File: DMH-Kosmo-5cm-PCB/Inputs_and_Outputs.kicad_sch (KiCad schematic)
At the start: 7 parts, among them J1 TS_Jack_6.35mm_Sw, J2 TS_Jack_6.35mm_Sw, J200 IDC_02x05, J3 TS_Jack_6.35mm_Sw, J4 TS_Jack_6.35mm_Sw, J50 Conn_01x06, J60 Conn_01x06

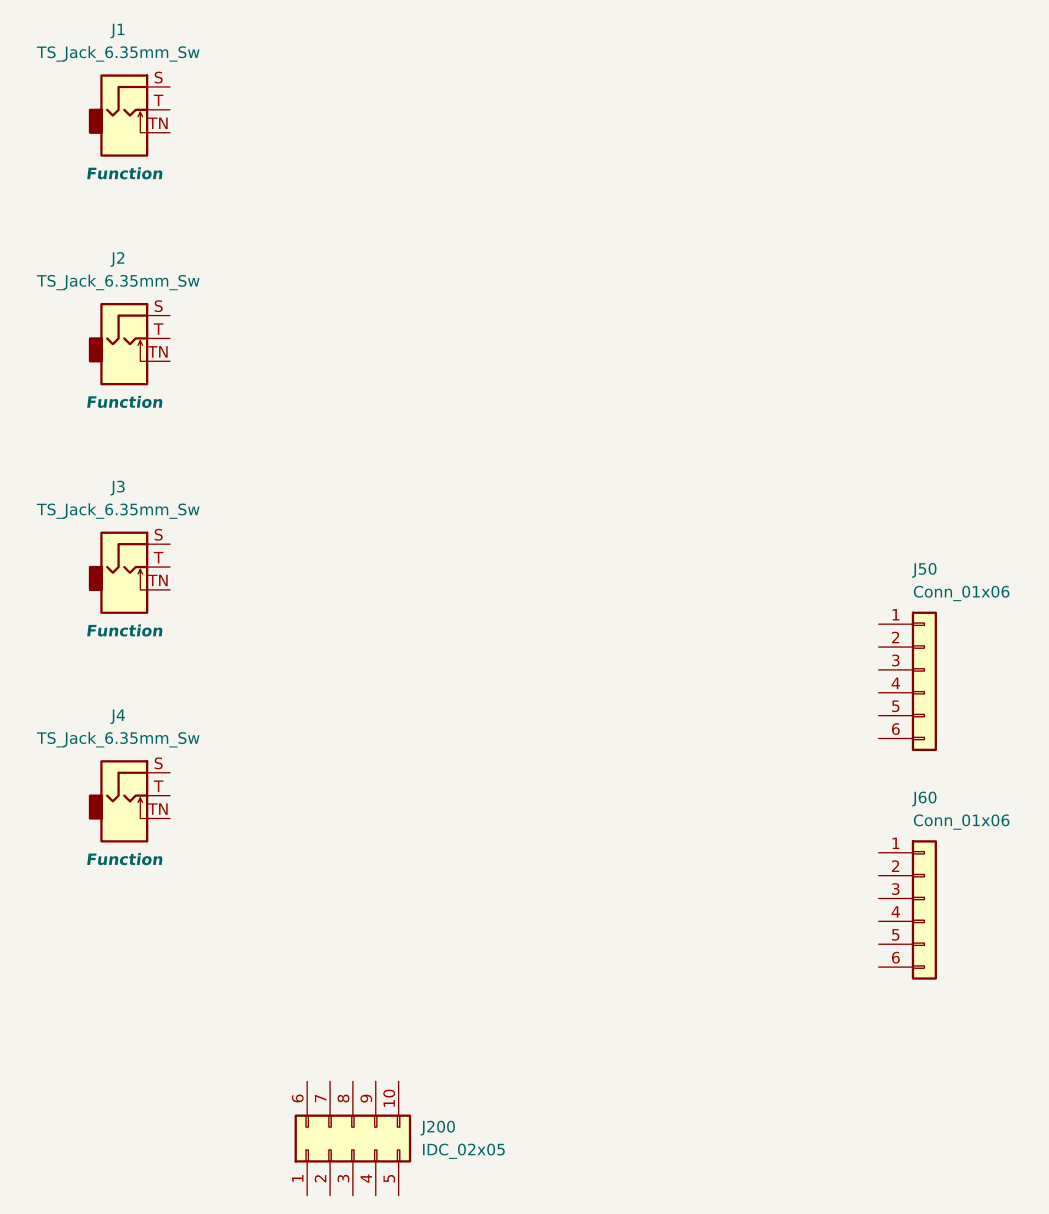
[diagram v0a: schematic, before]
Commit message: Enlarged PCB limits
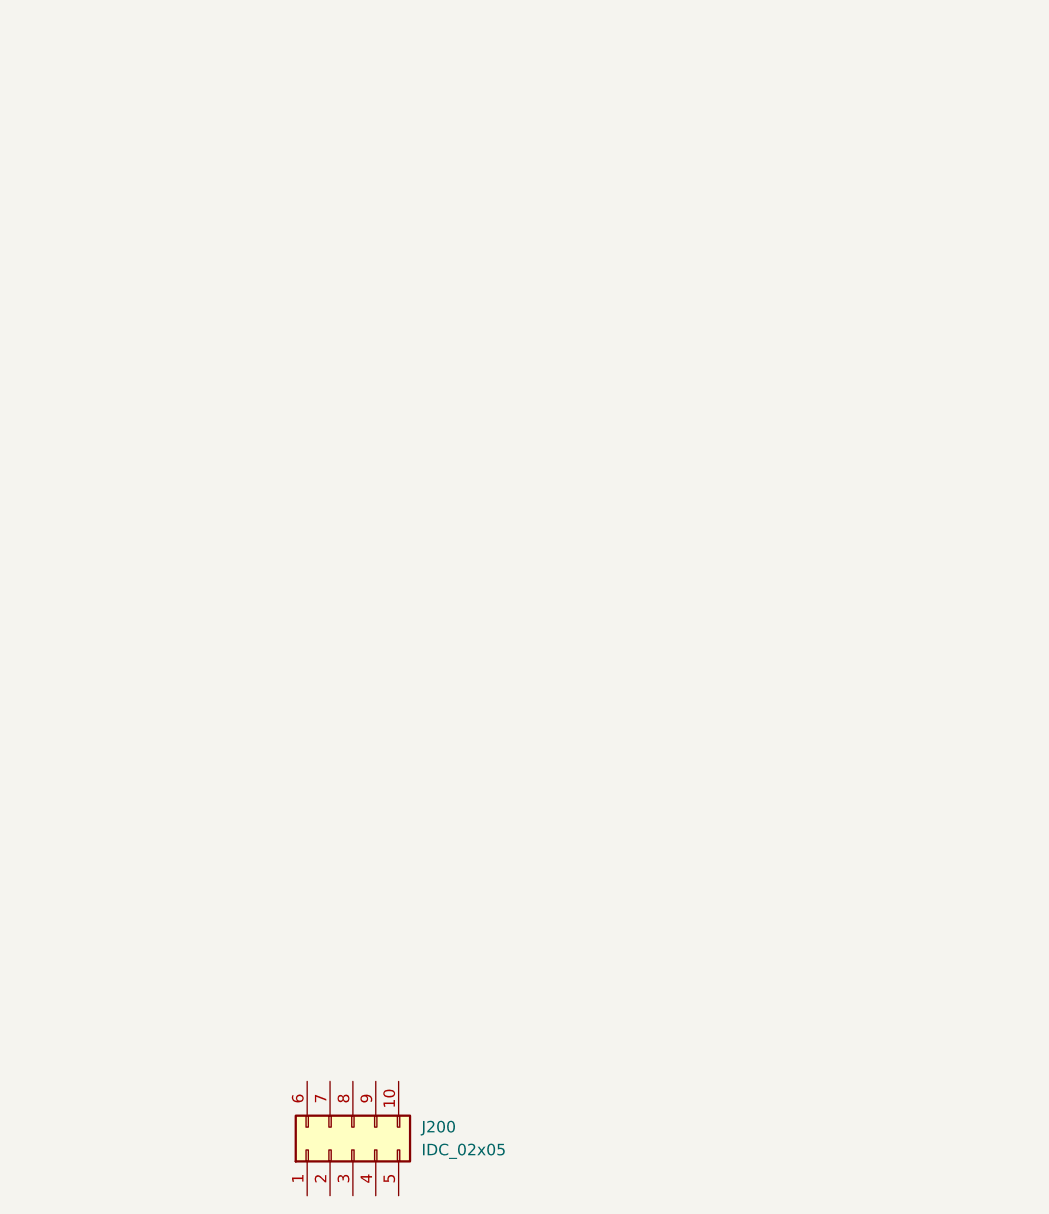
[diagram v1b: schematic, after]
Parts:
- removed J1, J2, J3, J4: TS_Jack_6.35mm_Sw, SynthStuff:CUI_MJ-63052A, symbol SynthStuff:TS_Jack_6.35mm_Sw
- removed J50, J60: Conn_01x06, Connector_PinSocket_2.54mm:PinSocket_1x06_P2.54mm_Vertical, symbol Connector_Generic:Conn_01x06
